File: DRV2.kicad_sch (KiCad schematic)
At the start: 15 parts

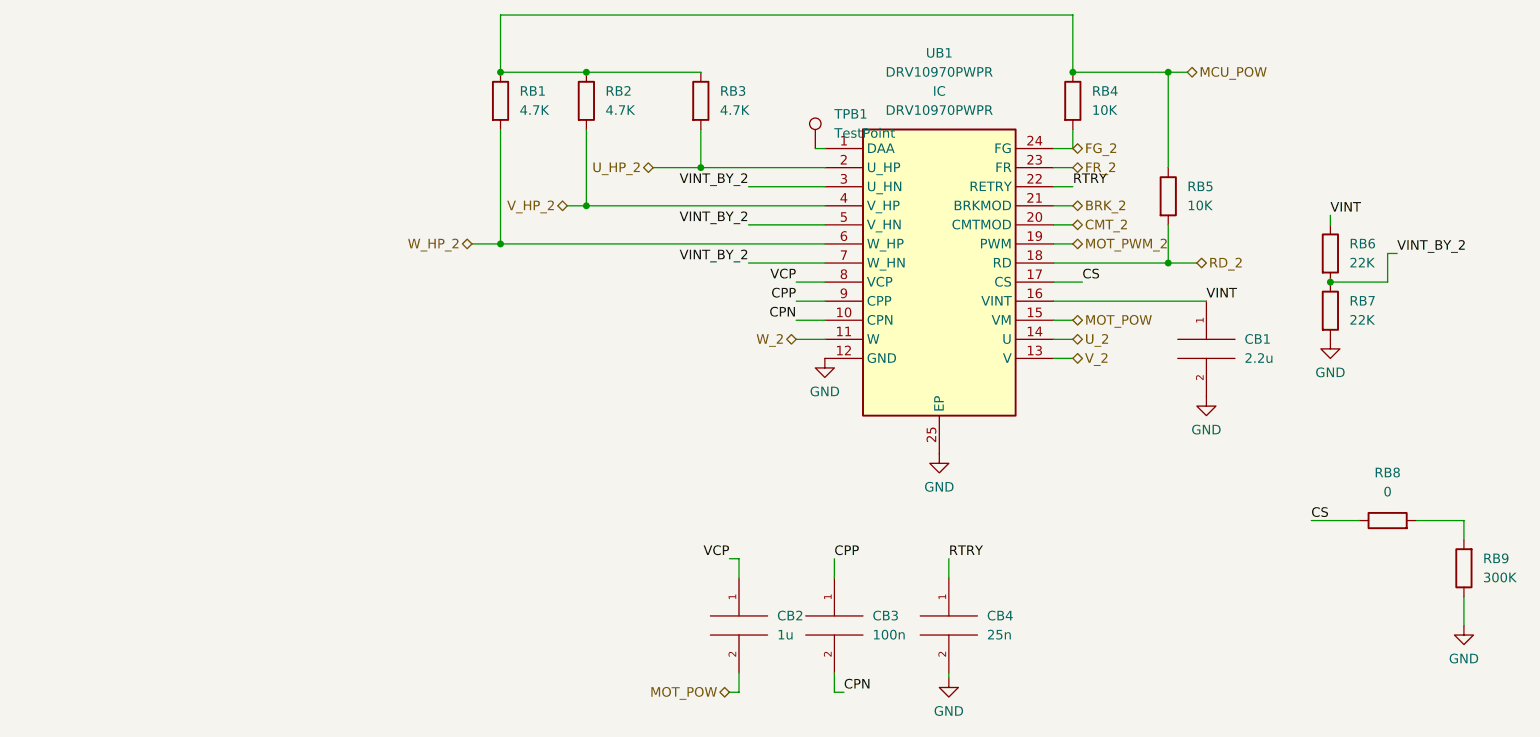
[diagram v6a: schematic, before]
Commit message: Page settings changed. Added some testpoints. Some comments are made.
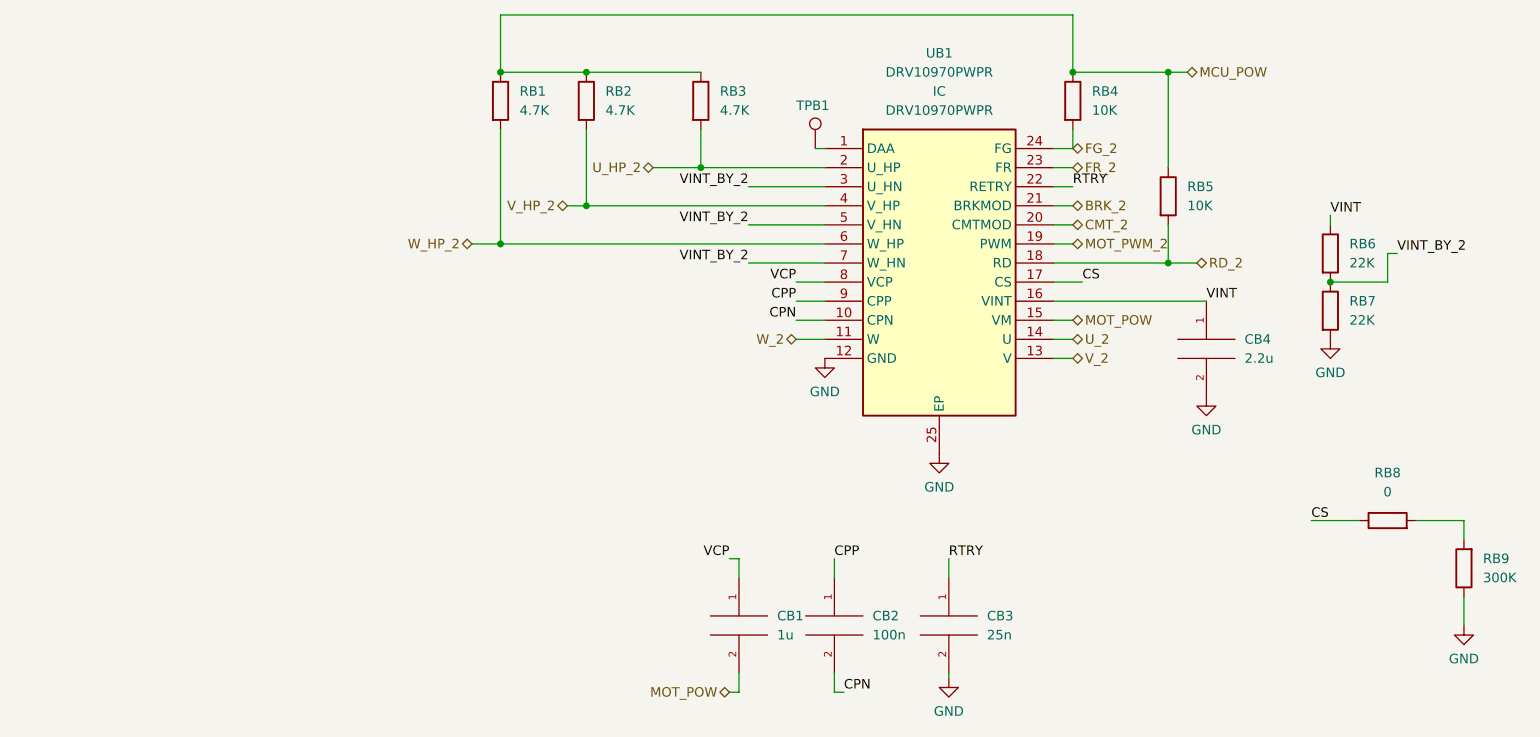
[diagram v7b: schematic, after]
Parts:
- TPB1: footprint (none) -> TestPoint:TestPoint_Plated_Hole_D2.0mm
- renumbered CB2 to CB1, CB3 to CB2, CB4 to CB3, CB1 to CB4
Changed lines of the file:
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@@
   (symbol (lib_id "pspice:C") (at 115.57 135.89 0) (unit 1)
     (in_bom yes) (on_board yes) (fields_autoplaced)
-    (property "Reference" "CB2" (id 0) (at 120.65 134.6199 0)
+    (property "Reference" "CB1" (id 0) (at 120.65 134.6199 0)
       (effects (font (size 1.27 1.27)) (justify left))
     )
@@
   (symbol (lib_id "upsat-comms-hardware:GND") (at 177.8 105.41 0) (unit 1)
     (in_bom yes) (on_board yes) (fields_autoplaced)
-    (property "Reference" "#PWR072" (id 0) (at 177.8 111.76 0)
+    (property "Reference" "#PWR086" (id 0) (at 177.8 111.76 0)
       (effects (font (size 1.27 1.27)) hide)
     )
@@
     (pin "2")
   )
+  (symbol (lib_id "Connector:TestPoint") (at 125.73 72.39 0) (unit 1)
+    (in_bom yes) (on_board yes)
+    (property "Reference" "TPB1" (id 0) (at 123.19 66.675 0)
+      (effects (font (size 1.27 1.27)) (justify left))
+    )
+    (property "Value" "TestPoint" (id 1) (at 121.285 66.675 0)
+      (effects (font (size 1.27 1.27)) (justify left) hide)
+    )
+    (property "Footprint" "TestPoint:TestPoint_Plated_Hole_D2.0mm" (id 2) (at 130.81 72.39 0)
+      (effects (font (size 1.27 1.27)) hide)
+    )
+    (property "Datasheet" "~" (id 3) (at 130.81 72.39 0)
+      (effects (font (size 1.27 1.27)) hide)
+    )
+    (pin "1")
+  )
   (symbol (lib_id "Device:R") (at 194.31 86.36 0) (unit 1)
     (in_bom yes) (on_board yes) (fields_autoplaced)
@@
   (symbol (lib_id "upsat-comms-hardware:GND") (at 194.31 97.79 0) (unit 1)
     (in_bom yes) (on_board yes) (fields_autoplaced)
-    (property "Reference" "#PWR070" (id 0) (at 194.31 104.14 0)
+    (property "Reference" "#PWR087" (id 0) (at 194.31 104.14 0)
       (effects (font (size 1.27 1.27)) hide)
     )
@@
   (symbol (lib_id "upsat-comms-hardware:GND") (at 143.51 142.875 0) (unit 1)
     (in_bom yes) (on_board yes) (fields_autoplaced)
-    (property "Reference" "#PWR075" (id 0) (at 143.51 149.225 0)
+    (property "Reference" "#PWR085" (id 0) (at 143.51 149.225 0)
       (effects (font (size 1.27 1.27)) hide)
     )
@@
   (symbol (lib_id "upsat-comms-hardware:GND") (at 127 100.33 0) (unit 1)
     (in_bom yes) (on_board yes) (fields_autoplaced)
-    (property "Reference" "#PWR071" (id 0) (at 127 106.68 0)
+    (property "Reference" "#PWR083" (id 0) (at 127 106.68 0)
       (effects (font (size 1.27 1.27)) hide)
     )
@@
   (symbol (lib_id "upsat-comms-hardware:GND") (at 212.09 135.89 0) (unit 1)
     (in_bom yes) (on_board yes) (fields_autoplaced)
-    (property "Reference" "#PWR074" (id 0) (at 212.09 142.24 0)
+    (property "Reference" "#PWR088" (id 0) (at 212.09 142.24 0)
       (effects (font (size 1.27 1.27)) hide)
     )
@@
   (symbol (lib_id "pspice:C") (at 128.27 135.89 0) (unit 1)
     (in_bom yes) (on_board yes) (fields_autoplaced)
-    (property "Reference" "CB3" (id 0) (at 133.35 134.6199 0)
+    (property "Reference" "CB2" (id 0) (at 133.35 134.6199 0)
       (effects (font (size 1.27 1.27)) (justify left))
     )
@@
   (symbol (lib_id "upsat-comms-hardware:GND") (at 142.24 113.03 0) (unit 1)
     (in_bom yes) (on_board yes) (fields_autoplaced)
-    (property "Reference" "#PWR073" (id 0) (at 142.24 119.38 0)
+    (property "Reference" "#PWR084" (id 0) (at 142.24 119.38 0)
       (effects (font (size 1.27 1.27)) hide)
     )
@@
   (symbol (lib_id "pspice:C") (at 177.8 99.06 0) (unit 1)
     (in_bom yes) (on_board yes) (fields_autoplaced)
-    (property "Reference" "CB1" (id 0) (at 182.88 97.7899 0)
+    (property "Reference" "CB4" (id 0) (at 182.88 97.7899 0)
       (effects (font (size 1.27 1.27)) (justify left))
     )
@@
   (symbol (lib_id "pspice:C") (at 143.51 135.89 0) (unit 1)
     (in_bom yes) (on_board yes) (fields_autoplaced)
-    (property "Reference" "CB4" (id 0) (at 148.59 134.6199 0)
+    (property "Reference" "CB3" (id 0) (at 148.59 134.6199 0)
       (effects (font (size 1.27 1.27)) (justify left))
     )
@@
     (pin "2")
   )
-  (symbol (lib_id "Connector:TestPoint") (at 125.73 72.39 0) (unit 1)
-    (in_bom yes) (on_board yes) (fields_autoplaced)
-    (property "Reference" "TPB1" (id 0) (at 128.27 67.8179 0)
-      (effects (font (size 1.27 1.27)) (justify left))
-    )
-    (property "Value" "TestPoint" (id 1) (at 128.27 70.3579 0)
-      (effects (font (size 1.27 1.27)) (justify left))
-    )
-    (property "Footprint" "" (id 2) (at 130.81 72.39 0)
-      (effects (font (size 1.27 1.27)) hide)
-    )
-    (property "Datasheet" "~" (id 3) (at 130.81 72.39 0)
-      (effects (font (size 1.27 1.27)) hide)
-    )
-    (pin "1")
-  )
   (symbol (lib_id "Device:R") (at 160.02 66.04 0) (unit 1)

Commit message: I2C lines are pulled up
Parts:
- CB1, CB2, CB3, CB4: footprint (none) -> Capacitor_SMD:C_0603_1608Metric
- RB1, RB2, RB3, RB4, RB5, RB6, RB7, RB8, RB9: footprint (none) -> Resistor_SMD:R_0603_1608Metric
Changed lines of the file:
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@@
     (property "Reference" "RB8" (id 0) (at 201.93 115.57 90))
     (property "Value" "0" (id 1) (at 201.93 118.11 90))
-    (property "Footprint" "" (id 2) (at 201.93 123.698 90)
+    (property "Footprint" "Resistor_SMD:R_0603_1608Metric" (id 2) (at 201.93 123.698 90)
       (effects (font (size 1.27 1.27)) hide)
     )
@@
       (effects (font (size 1.27 1.27)) (justify left))
     )
-    (property "Footprint" "" (id 2) (at 115.57 135.89 0)
+    (property "Footprint" "Capacitor_SMD:C_0603_1608Metric" (id 2) (at 115.57 135.89 0)
       (effects (font (size 1.27 1.27)) hide)
     )
@@
       (effects (font (size 1.27 1.27)) (justify left))
     )
-    (property "Footprint" "" (id 2) (at 82.042 66.04 90)
+    (property "Footprint" "Resistor_SMD:R_0603_1608Metric" (id 2) (at 82.042 66.04 90)
       (effects (font (size 1.27 1.27)) hide)
     )
@@
   (symbol (lib_id "upsat-comms-hardware:GND") (at 177.8 105.41 0) (unit 1)
     (in_bom yes) (on_board yes) (fields_autoplaced)
-    (property "Reference" "#PWR086" (id 0) (at 177.8 111.76 0)
+    (property "Reference" "#PWR087" (id 0) (at 177.8 111.76 0)
       (effects (font (size 1.27 1.27)) hide)
     )
@@
       (effects (font (size 1.27 1.27)) (justify left))
     )
-    (property "Footprint" "" (id 2) (at 108.712 66.04 90)
+    (property "Footprint" "Resistor_SMD:R_0603_1608Metric" (id 2) (at 108.712 66.04 90)
       (effects (font (size 1.27 1.27)) hide)
     )
@@
       (effects (font (size 1.27 1.27)) (justify left))
     )
-    (property "Footprint" "" (id 2) (at 192.532 86.36 90)
+    (property "Footprint" "Resistor_SMD:R_0603_1608Metric" (id 2) (at 192.532 86.36 90)
       (effects (font (size 1.27 1.27)) hide)
     )
@@
       (effects (font (size 1.27 1.27)) (justify left))
     )
-    (property "Footprint" "" (id 2) (at 170.942 78.74 90)
+    (property "Footprint" "Resistor_SMD:R_0603_1608Metric" (id 2) (at 170.942 78.74 90)
       (effects (font (size 1.27 1.27)) hide)
     )
@@
   (symbol (lib_id "upsat-comms-hardware:GND") (at 194.31 97.79 0) (unit 1)
     (in_bom yes) (on_board yes) (fields_autoplaced)
-    (property "Reference" "#PWR087" (id 0) (at 194.31 104.14 0)
+    (property "Reference" "#PWR088" (id 0) (at 194.31 104.14 0)
       (effects (font (size 1.27 1.27)) hide)
     )
@@
   (symbol (lib_id "upsat-comms-hardware:GND") (at 143.51 142.875 0) (unit 1)
     (in_bom yes) (on_board yes) (fields_autoplaced)
-    (property "Reference" "#PWR085" (id 0) (at 143.51 149.225 0)
+    (property "Reference" "#PWR086" (id 0) (at 143.51 149.225 0)
       (effects (font (size 1.27 1.27)) hide)
     )
@@
   (symbol (lib_id "upsat-comms-hardware:GND") (at 127 100.33 0) (unit 1)
     (in_bom yes) (on_board yes) (fields_autoplaced)
-    (property "Reference" "#PWR083" (id 0) (at 127 106.68 0)
+    (property "Reference" "#PWR084" (id 0) (at 127 106.68 0)
       (effects (font (size 1.27 1.27)) hide)
     )
@@
   (symbol (lib_id "upsat-comms-hardware:GND") (at 212.09 135.89 0) (unit 1)
     (in_bom yes) (on_board yes) (fields_autoplaced)
-    (property "Reference" "#PWR088" (id 0) (at 212.09 142.24 0)
+    (property "Reference" "#PWR089" (id 0) (at 212.09 142.24 0)
       (effects (font (size 1.27 1.27)) hide)
     )
@@
       (effects (font (size 1.27 1.27)) (justify left))
     )
-    (property "Footprint" "" (id 2) (at 128.27 135.89 0)
+    (property "Footprint" "Capacitor_SMD:C_0603_1608Metric" (id 2) (at 128.27 135.89 0)
       (effects (font (size 1.27 1.27)) hide)
     )
@@
       (effects (font (size 1.27 1.27)) (justify left))
     )
-    (property "Footprint" "" (id 2) (at 93.472 66.04 90)
+    (property "Footprint" "Resistor_SMD:R_0603_1608Metric" (id 2) (at 93.472 66.04 90)
       (effects (font (size 1.27 1.27)) hide)
     )
@@
       (effects (font (size 1.27 1.27)) (justify left))
     )
-    (property "Footprint" "" (id 2) (at 192.532 93.98 90)
+    (property "Footprint" "Resistor_SMD:R_0603_1608Metric" (id 2) (at 192.532 93.98 90)
       (effects (font (size 1.27 1.27)) hide)
     )
@@
   (symbol (lib_id "upsat-comms-hardware:GND") (at 142.24 113.03 0) (unit 1)
     (in_bom yes) (on_board yes) (fields_autoplaced)
-    (property "Reference" "#PWR084" (id 0) (at 142.24 119.38 0)
+    (property "Reference" "#PWR085" (id 0) (at 142.24 119.38 0)
       (effects (font (size 1.27 1.27)) hide)
     )
@@
       (effects (font (size 1.27 1.27)) (justify left))
     )
-    (property "Footprint" "" (id 2) (at 177.8 99.06 0)
+    (property "Footprint" "Capacitor_SMD:C_0603_1608Metric" (id 2) (at 177.8 99.06 0)
       (effects (font (size 1.27 1.27)) hide)
     )
@@
       (effects (font (size 1.27 1.27)) (justify left))
     )
-    (property "Footprint" "" (id 2) (at 143.51 135.89 0)
+    (property "Footprint" "Capacitor_SMD:C_0603_1608Metric" (id 2) (at 143.51 135.89 0)
       (effects (font (size 1.27 1.27)) hide)
     )
@@
       (effects (font (size 1.27 1.27)) (justify left))
     )
-    (property "Footprint" "" (id 2) (at 158.242 66.04 90)
+    (property "Footprint" "Resistor_SMD:R_0603_1608Metric" (id 2) (at 158.242 66.04 90)
       (effects (font (size 1.27 1.27)) hide)
     )
@@
       (effects (font (size 1.27 1.27)) (justify right))
     )
-    (property "Footprint" "" (id 2) (at 213.868 128.27 90)
-      (effects (font (size 1.27 1.27)) hide)
-    )
+    (property "Footprint" "Resistor_SMD:R_0603_1608Metric" (id 2) (at 213.868 128.27 90)
+      (effects (font (size 1.27 1.27)) hide)
+    )
